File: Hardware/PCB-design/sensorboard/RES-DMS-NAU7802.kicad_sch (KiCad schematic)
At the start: 43 parts, among them J1 Conn_01x06, J2 straingauge, J4 straingauge, J5 straingauge, J6 straingauge, U1 NAU7802-SGI

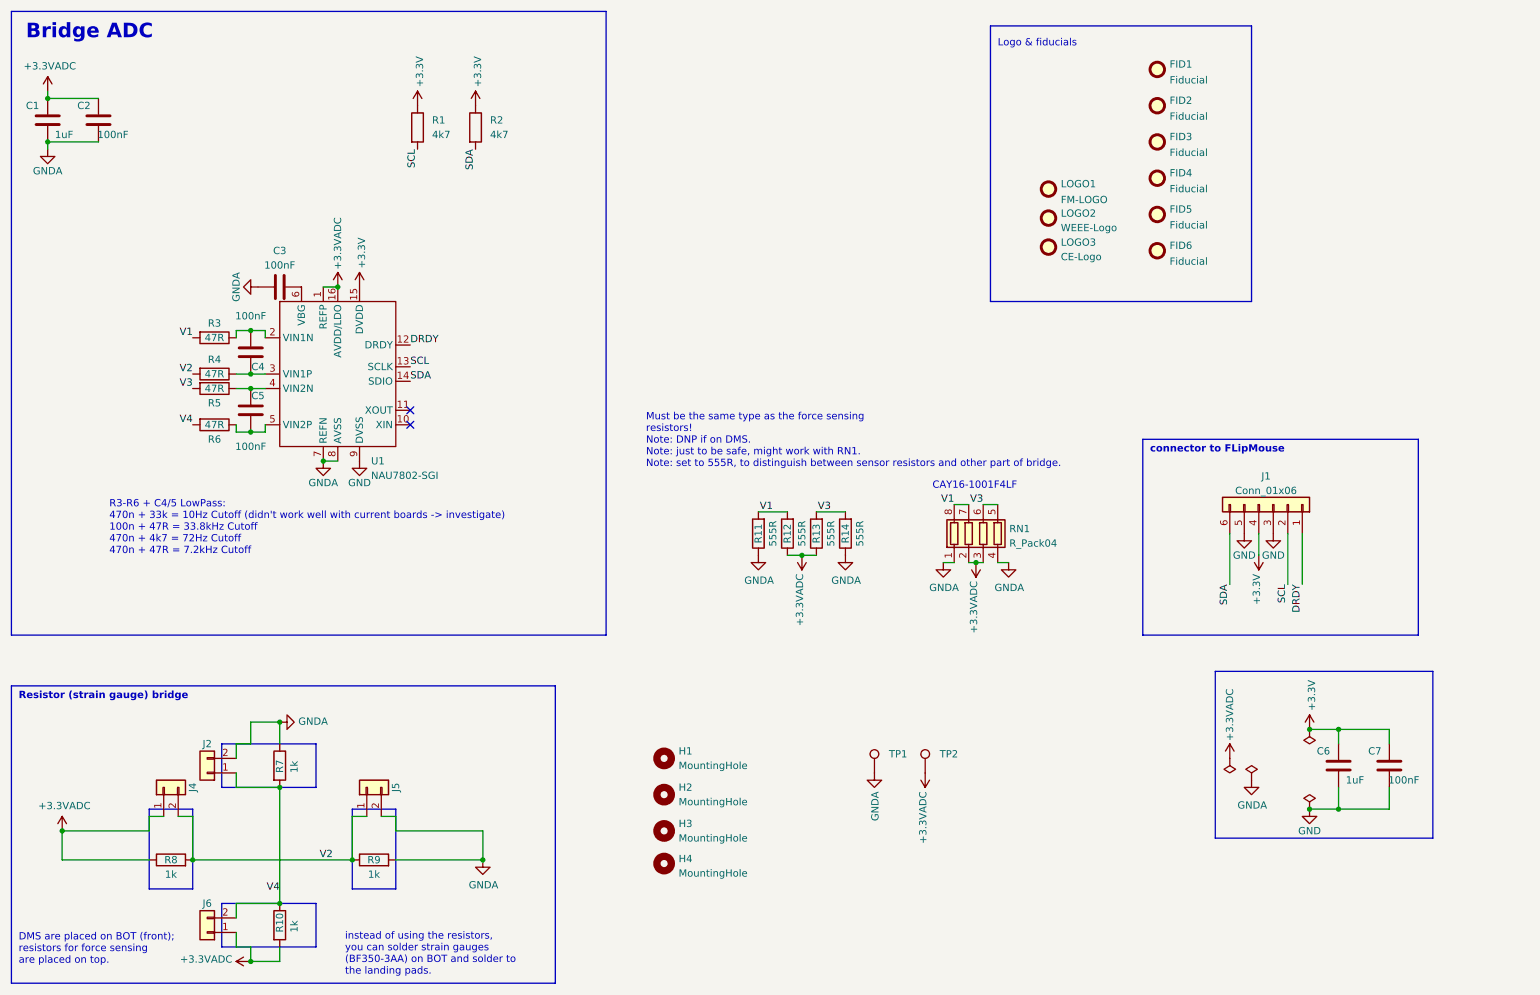
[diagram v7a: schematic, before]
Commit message: Added BOM File, changed resistors in sensorboard to DNP
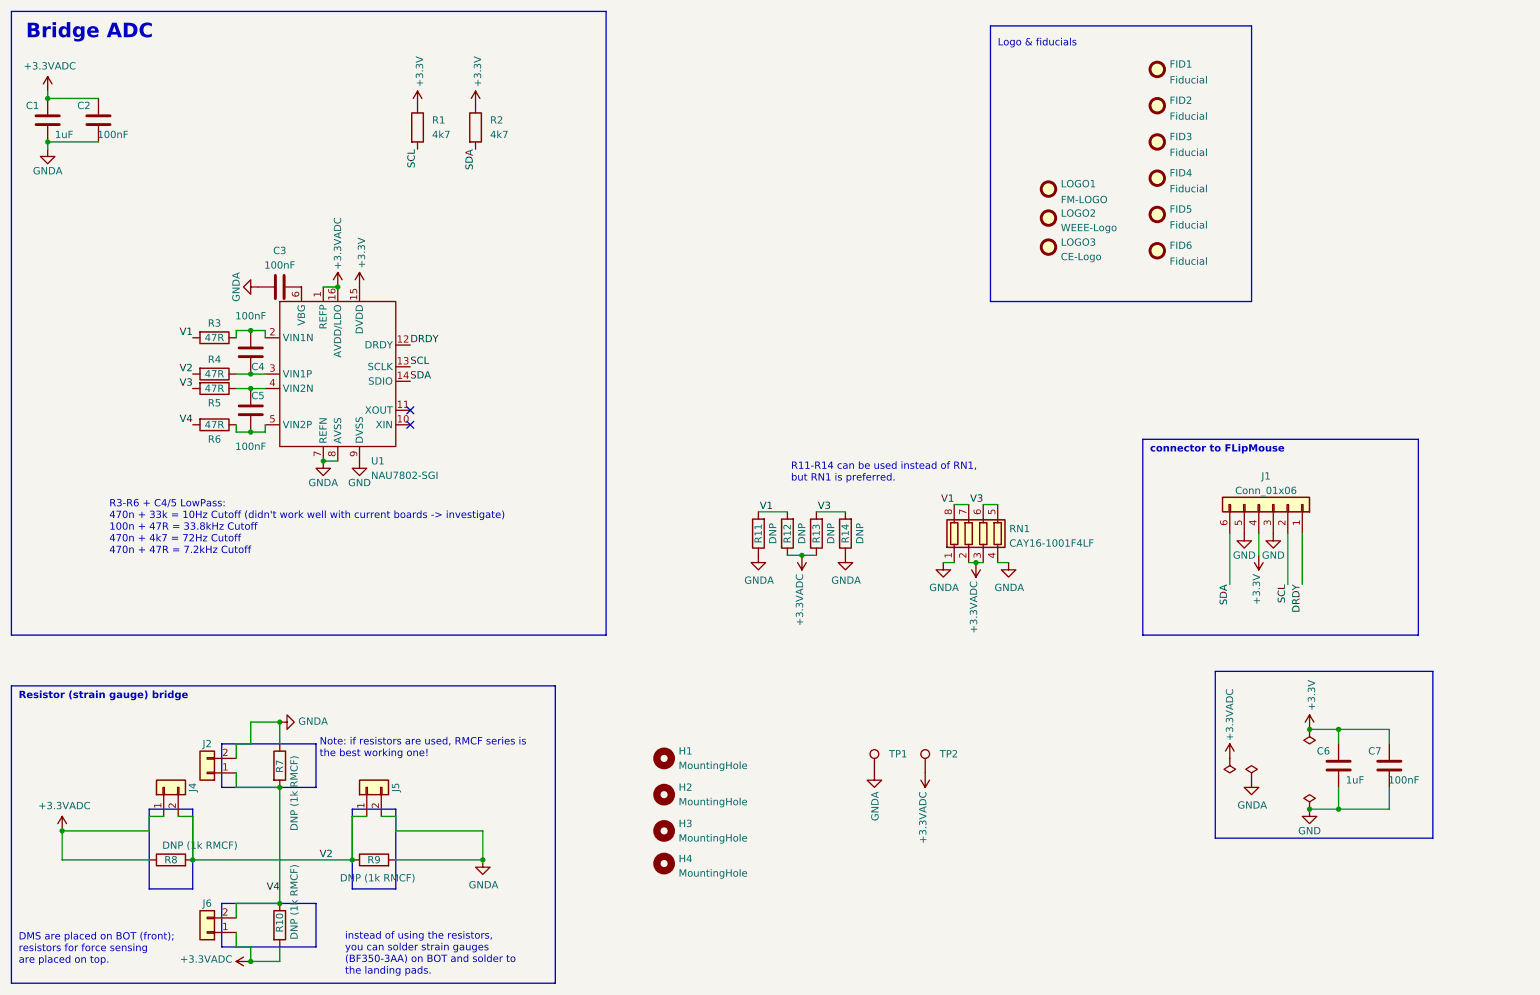
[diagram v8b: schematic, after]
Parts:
- C1, C6: Digikey (none) -> 1276-6524-1-ND; Farnell (none) -> 3013384; Mouser (none) -> 581-06036C105MAT2A; RS-Components (none) -> 184-3898
- C2, C3, C4, C5, C7: Digikey (none) -> 1276-CL10B104KB8NNNLCT-ND; Farnell (none) -> 3013409; Mouser (none) -> 581-06035C104K4; RS-Components (none) -> 200-6519
- J1: Digikey (none) -> 732-1965-1-ND; Farnell (none) -> 1641849; Mouser (none) -> 710-690367280676; RS-Components (none) -> 771-8109
- R1, R2: Digikey (none) -> 1292-WR06X472JTLCT-ND; Farnell (none) -> 3994558; Mouser (none) -> 756-WCR0603-4K7FI; RS-Components (none) -> 199-5594
- R10, R7, R9: value 1k -> DNP (1k RMCF)
- R11, R12, R13, R14: value 555R -> DNP
- R3, R4, R5, R6: Digikey (none) -> P47.0HCT-ND; Farnell (none) -> 2447378; Mouser (none) -> 603-RC0603JR-1347RL; RS-Components (none) -> 199-5584
- R8: value 1k -> DNP (1k RMCF); Farnell 2447473 -> (none)
- RN1: value R_Pack04 -> CAY16-1001F4LF; Digikey (none) -> CAY16-1001F4LFCT-ND; Farnell (none) -> 1770141; Mouser (none) -> 652-CAY16-1001F4LF; RS-Components (none) -> 181-4454
- U1: Digikey (none) -> NAU7802SGI-ND; Farnell (none) -> --; Mouser (none) -> --; RS-Components (none) -> --
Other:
- note added: "Note: if resistors are used, RMCF series is the best working one!"
- note added: "R11-R14 can be used instead of RN1, but RN1 is preferred."
- note removed: "CAY16-1001F4LF"
- note removed: "Must be the same type as the force sensing resistors! Note: DNP if on DMS. Note: just to be safe, might work with RN1. Note: set to 555R, to distinguish between sensor resistors and other part of bridge."
